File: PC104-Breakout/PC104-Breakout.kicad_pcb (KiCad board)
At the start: 4 copper layers, 175 x 100 mm, 21 parts, among them J1 Screw_Terminal_01x02, J2 Screw_Terminal_01x02, J3 Screw_Terminal_01x02, M1 MountingHole_Pad, M2 MountingHole_Pad, M3 MountingHole_Pad, M4 MountingHole_Pad, M5 MountingHole_Pad, M6 MountingHole_Pad, M7 MountingHole_Pad, M8 MountingHole_Pad

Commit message: Added silkscreen - created production files
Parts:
- added G***: LOGO, LOGO, B.Cu at (208.2, 95.7)
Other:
- board text added: "2024-05-20"
- board text added: "Rev 1"

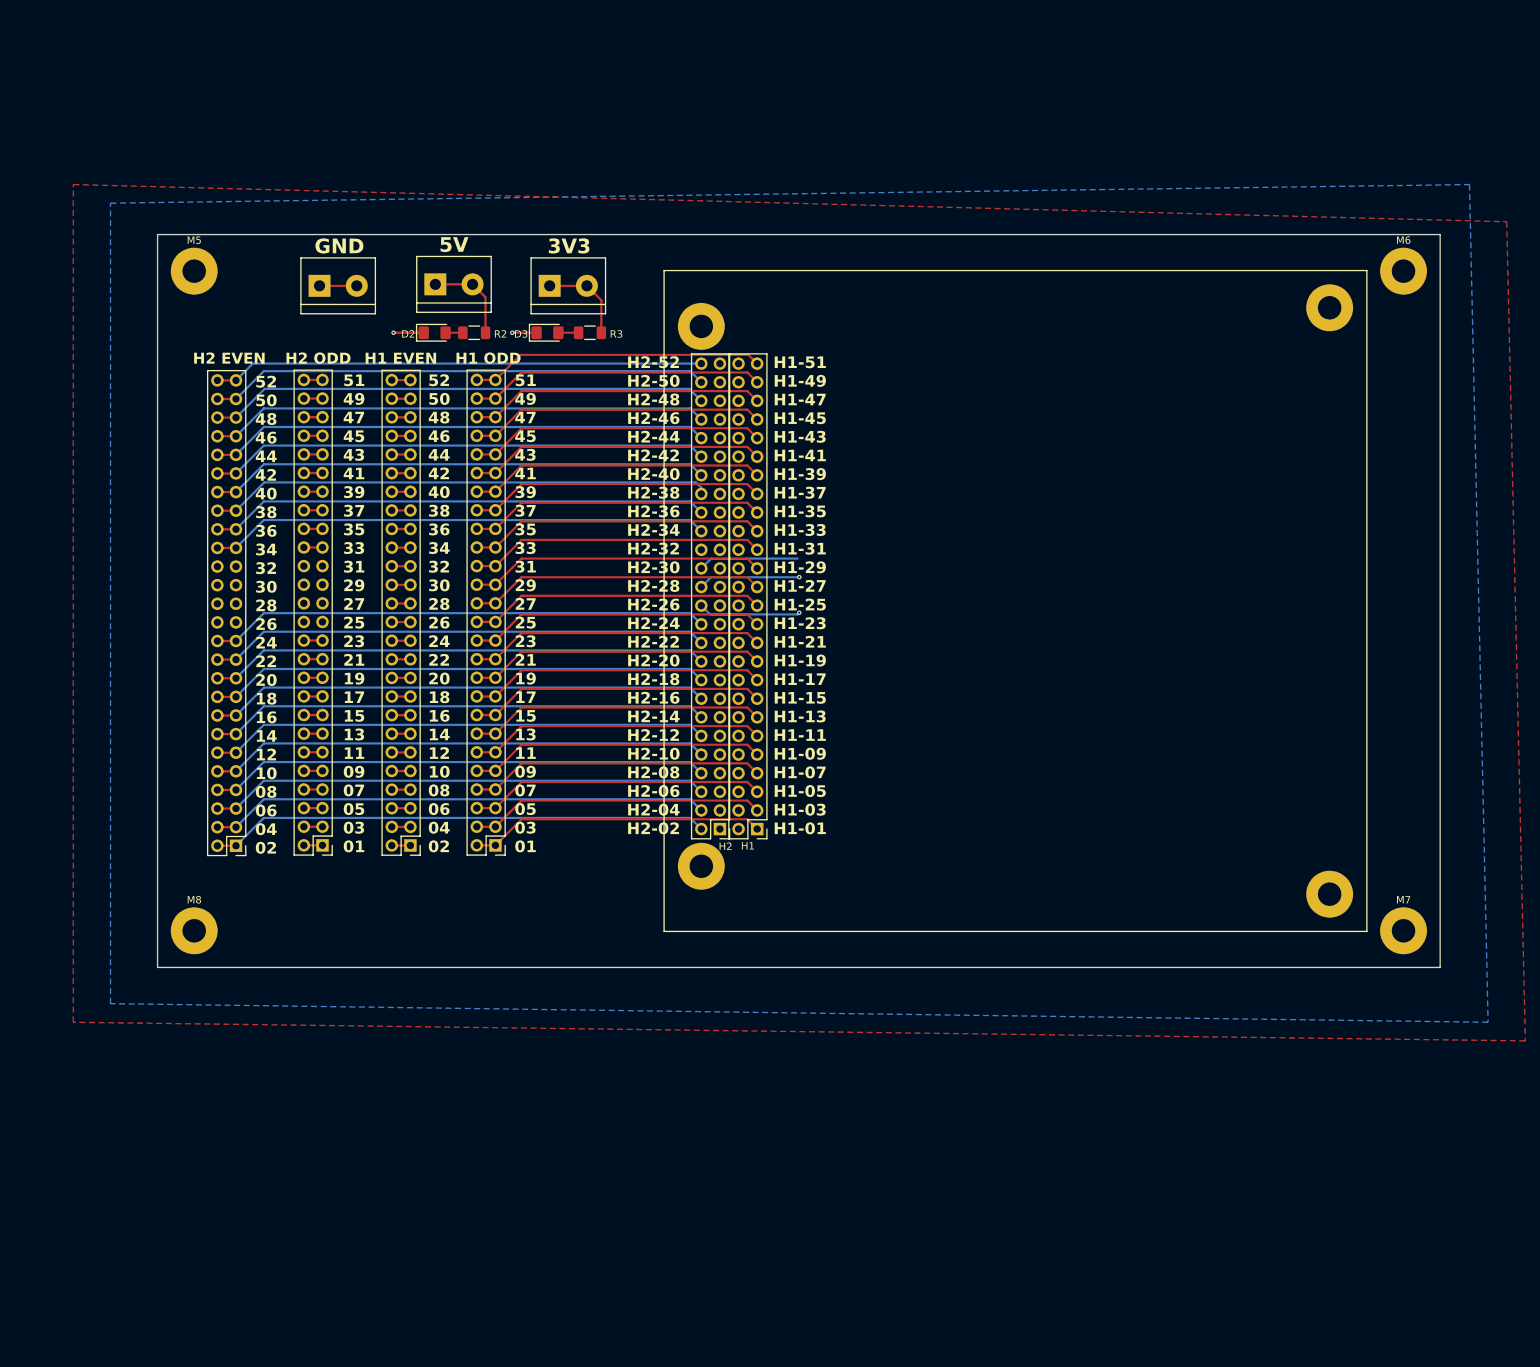
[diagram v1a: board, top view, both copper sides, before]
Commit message: Reorganized PCB layout
Modified layout files to change board from 4 layers to 2 in order to decrease production costs by $45. Shifted two stack headers to the right of the space allocated for the EPS and rerouted with 2 layers. Created polygons for GND and 3V3 nets.
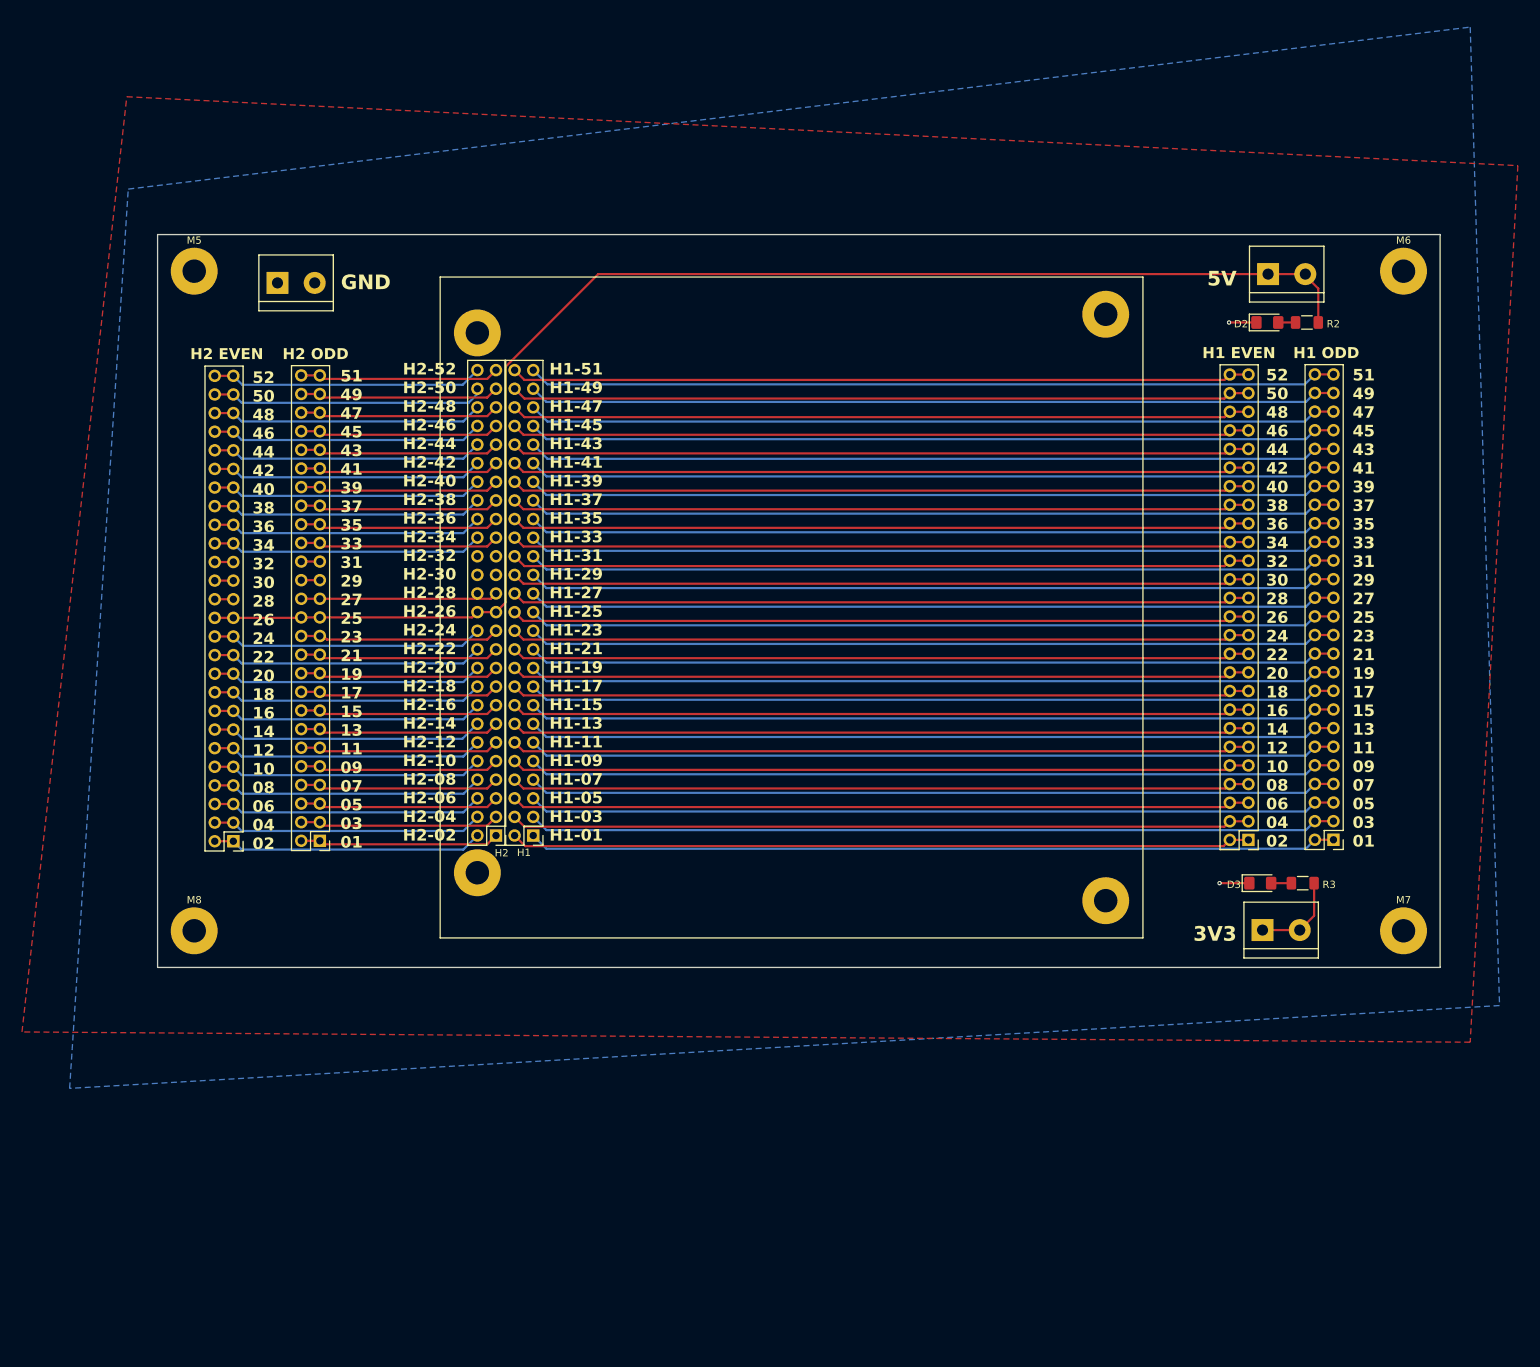
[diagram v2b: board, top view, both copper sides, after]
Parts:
- moved J3 131.1 mm to (225.8, 144.9)
- moved D3 122.9 mm to (225.4, 138.5)
- moved R3 122.9 mm to (231.2, 138.5)
- moved H1E1 114.3 mm to (223.8, 132.6)
- moved H1O1 114.3 mm to (235.4, 132.6)
- moved J2 113.6 mm to (226.5, 55.4)
- moved D2 113.6 mm to (226.4, 62.0)
- moved R2 113.6 mm to (231.8, 62.0)
- moved G*** 30.6 mm to (177.6, 96.6)
- moved H1 30.6 mm to (126.3, 132.0)
- moved H2 30.6 mm to (121.2, 132.0)
- moved M1 30.6 mm to (118.6, 63.4)
- moved M4 30.6 mm to (118.6, 137.1)
- moved M2 30.6 mm to (204.4, 60.9)
- moved M3 30.6 mm to (204.4, 140.9)
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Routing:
- net H2-25: track 26.4 -> 194.4 mm, vias 1 -> 0
- net H1-51: track 40.2 -> 110.6 mm
- net H1-43: track 40.3 -> 110.6 mm
- net H1-47: track 40.3 -> 110.6 mm
- net H1-07: track 40.3 -> 110.4 mm
- net H1-39: track 40.3 -> 110.4 mm
- net H1-49: track 40.3 -> 110.4 mm
- net H1-45: track 40.3 -> 110.4 mm
- net H1-37: track 40.3 -> 110.4 mm
- net H1-35: track 40.3 -> 110.4 mm
- net H1-33: track 40.3 -> 110.4 mm
- net H1-31: track 40.3 -> 110.4 mm
- net H1-29: track 40.3 -> 110.4 mm
- net H1-27: track 40.3 -> 110.4 mm
- net H1-25: track 40.3 -> 110.4 mm
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- added copper zone on F.Cu, net H2-27
- removed copper zone on F.Cu, net H2-25
- removed copper zone on In1.Cu, net H2-27
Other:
- copper layers 4 -> 2

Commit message: Completed layout, updated silkscreen and added aesthetic fixes
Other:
- board text added: "2024-05-21"
- board text added: "Rev 2"
- board text removed: "2024-05-20"
- board text removed: "Rev 1"
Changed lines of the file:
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@@
 		(layer "Edge.Cuts")
 	)
-	(gr_text "2024-05-20\n"
+	(gr_text "2024-05-21\n"
 		(at 189.645 116.485 0)
 		(layer "B.SilkS")
@@
 		)
 	)
-	(gr_text "Rev 1"
-		(at 181.245 109.685 0)
+	(gr_text "Rev 2"
+		(at 181.245 108.7 0)
 		(layer "B.SilkS")
 		(effects

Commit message: Created production files
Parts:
- removed the G*** at (177.6, 96.6)
- added G***: LOGO, PC104-Breakout-Lib:CTS-Logo-50x25, B.Cu at (175.9, 95.0)
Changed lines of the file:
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@@
 		)
 	)
-	(footprint "LOGO"
+	(footprint "PC104-Breakout-Lib:CTS-Logo-50x25"
 		(layer "B.Cu")
-		(at 177.614973 96.585639 180)
+		(at 175.9 95 180)
 		(property "Reference" "G***"
 			(at 0 0 180)
@@
 			)
 		)
-		(property "Footprint" ""
+		(property "Footprint" "PC104-Breakout-Lib:CTS-Logo-50x25"
 			(at 0 0 0)
 			(unlocked yes)
@@
 	)
 	(gr_text "Rev 2"
-		(at 181.245 108.7 0)
+		(at 181.245 108.4 0)
 		(layer "B.SilkS")
 		(effects
@@
 	)
 	(segment
-		(start 122.515 68.002943)
-		(end 135.117943 55.4)
-		(width 0.3)
+		(start 226.52 55.4)
+		(end 134.8 55.4)
+		(width 1)
 		(layer "F.Cu")
 		(net 56)
 	)
 	(segment
-		(start 231.6 55.6)
-		(end 233.37 57.37)
+		(start 122.515 68.002943)
+		(end 122.515 67.685)
 		(width 0.3)
 		(layer "F.Cu")
@@
 	)
 	(segment
-		(start 226.52 55.4)
+		(start 233.37 57.17)
 		(end 231.6 55.4)
 		(width 0.3)
@@
 	)
 	(segment
-		(start 135.117943 55.4)
-		(end 226.52 55.4)
-		(width 0.3)
+		(start 134.8 55.4)
+		(end 125.1 65.1)
+		(width 1)
 		(layer "F.Cu")
 		(net 56)
@@
 	)
 	(segment
-		(start 233.37 57.37)
-		(end 233.37 62)
+		(start 231.6 55.4)
+		(end 226.52 55.4)
+		(width 1)
+		(layer "F.Cu")
+		(net 56)
+	)
+	(segment
+		(start 122.515 67.685)
+		(end 125.1 65.1)
 		(width 0.3)
 		(layer "F.Cu")
@@
 	)
 	(segment
+		(start 233.37 62)
+		(end 233.37 57.17)
+		(width 0.3)
+		(layer "F.Cu")
+		(net 56)
+	)
+	(segment
 		(start 117.915 102.24)
 		(end 118.635 101.52)
@@
 	)
 	(segment
-		(start 230.27 62)
-		(end 227.9075 62)
+		(start 227.9075 62)
+		(end 230.27 62)
 		(width 0.3)
 		(layer "F.Cu")

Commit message: Update for Rev 3, do layout
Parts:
- removed G***: LOGO, PC104-Breakout-Lib:CTS-Logo-50x25
- removed the J1 at (91.4, 56.6)
- removed the J2 at (226.5, 55.4)
- removed the J3 at (225.8, 144.9)
- added D1: LED, LED_SMD:LED_0603_1608Metric_Pad1.05x0.95mm_HandSolder, F.Cu at (220.6, 64.0)
- added D4: LED, LED_SMD:LED_0603_1608Metric_Pad1.05x0.95mm_HandSolder, F.Cu at (220.6, 71.8)
- added D5: LED, LED_SMD:LED_0603_1608Metric_Pad1.05x0.95mm_HandSolder, F.Cu at (220.6, 74.4)
- added D6: LED, LED_SMD:LED_0603_1608Metric_Pad1.05x0.95mm_HandSolder, F.Cu at (220.6, 77.0)
- added J4: Screw_Terminal_01x02, TerminalBlock:TerminalBlock_bornier-2_P5.08mm, F.Cu at (246.0, 143.5)
- added J5: Screw_Terminal_01x02, TerminalBlock:TerminalBlock_bornier-2_P5.08mm, F.Cu at (246.0, 108.0)
- added J6: Screw_Terminal_01x02, TerminalBlock:TerminalBlock_bornier-2_P5.08mm, F.Cu at (246.0, 72.0)
- added J7: Conn_01x02, Connector_PinHeader_2.54mm:PinHeader_1x03_P2.54mm_Vertical, F.Cu at (238.0, 143.5)
- added J8: Conn_01x02, Connector_PinHeader_2.54mm:PinHeader_1x03_P2.54mm_Vertical, F.Cu at (238.0, 108.5)
- added J9: Conn_01x02, Connector_PinHeader_2.54mm:PinHeader_1x03_P2.54mm_Vertical, F.Cu at (238.0, 72.0)
- added LG1: MountingHole, PC104-Breakout-Lib:CTS-Logo-50x25, B.Cu at (173.0, 93.0)
- added LG2: MountingHole, PC104-Breakout-Lib:CTS-Logo-50x25, F.Cu at (170.9, 92.5)
- added M10: MountingHole_Pad, MountingHole:MountingHole_3.2mm_M3_Pad, F.Cu at (213.0, 140.0)
- added M11: MountingHole_Pad, MountingHole:MountingHole_3.2mm_M3_Pad, F.Cu at (213.0, 61.0)
- added M12: MountingHole_Pad, MountingHole:MountingHole_3.2mm_M3_Pad, F.Cu at (110.0, 63.0)
- added M9: MountingHole_Pad, MountingHole:MountingHole_3.2mm_M3_Pad, F.Cu at (110.0, 140.0)
- added R1: 10k, Resistor_SMD:R_0603_1608Metric_Pad0.98x0.95mm_HandSolder, F.Cu at (85.0, 53.0)
- added R10: 5k1, Resistor_SMD:R_0603_1608Metric_Pad0.98x0.95mm_HandSolder, F.Cu at (224.9, 66.5)
- added R11: 3k3, Resistor_SMD:R_0603_1608Metric_Pad0.98x0.95mm_HandSolder, F.Cu at (224.9, 69.0)
- added R12: 3k3, Resistor_SMD:R_0603_1608Metric_Pad0.98x0.95mm_HandSolder, F.Cu at (224.9, 71.5)
- added R13: 10k, Resistor_SMD:R_0603_1608Metric_Pad0.98x0.95mm_HandSolder, F.Cu at (224.9, 74.0)
- added R14: 10k, Resistor_SMD:R_0603_1608Metric_Pad0.98x0.95mm_HandSolder, F.Cu at (224.9, 76.5)
- added R4: 10k, Resistor_SMD:R_0603_1608Metric_Pad0.98x0.95mm_HandSolder, F.Cu at (80.0, 169.0)
- added R5: 10k, Resistor_SMD:R_0603_1608Metric_Pad0.98x0.95mm_HandSolder, F.Cu at (110.0, 145.0)
- added R6: 10k, Resistor_SMD:R_0603_1608Metric_Pad0.98x0.95mm_HandSolder, F.Cu at (213.0, 135.0)
- added R7: 10k, Resistor_SMD:R_0603_1608Metric_Pad0.98x0.95mm_HandSolder, F.Cu at (213.0, 56.0)
- added R8: 10k, Resistor_SMD:R_0603_1608Metric_Pad0.98x0.95mm_HandSolder, F.Cu at (110.0, 58.0)
- added R9: 5k1, Resistor_SMD:R_0603_1608Metric_Pad0.98x0.95mm_HandSolder, F.Cu at (224.9, 64.0)
- added TP1: TestPoint, PC104-Breakout-Lib:EdgeAlligatorConnector, F.Cu at (236.0, 163.0)
- added TP2: TestPoint, PC104-Breakout-Lib:EdgeAlligatorConnector, F.Cu at (235.5, 128.0)
- added TP3: TestPoint, PC104-Breakout-Lib:EdgeAlligatorConnector, F.Cu at (235.5, 92.0)
- added TP4: TestPoint, PC104-Breakout-Lib:EdgeAlligatorConnector, F.Cu at (236.0, 152.0)
- added TP5: TestPoint, PC104-Breakout-Lib:EdgeAlligatorConnector, F.Cu at (235.5, 117.0)
- added TP6: TestPoint, PC104-Breakout-Lib:EdgeAlligatorConnector, F.Cu at (235.5, 81.0)
- D2, D3: value D -> LED; footprint Diode_SMD:D_1206_3216Metric_Pad1.42x1.75mm_HandSolder -> LED_SMD:LED_0603_1608Metric_Pad1.05x0.95mm_HandSolder
- R2: value 3.3k -> 10k; footprint Resistor_SMD:R_1206_3216Metric_Pad1.30x1.75mm_HandSolder -> Resistor_SMD:R_0603_1608Metric_Pad0.98x0.95mm_HandSolder
- R3: value 2.2k -> 10k; footprint Resistor_SMD:R_1206_3216Metric_Pad1.30x1.75mm_HandSolder -> Resistor_SMD:R_0603_1608Metric_Pad0.98x0.95mm_HandSolder
- moved J3 79.6 mm to (155.5, 170.5), turned to -90 degrees
- moved D3 69.5 mm to (220.6, 69.2)
- moved H3 63.0 mm to (155.5, 156.5), turned to -90 degrees
- moved J1 38.6 mm to (231.5, 170.5), turned to -90 degrees
- moved R3 36.6 mm to (240.0, 174.0), turned to 90 degrees
- moved M7 29.0 mm to (245.0, 174.0)
- moved M8 29.0 mm to (80.0, 174.0)
- moved J2 24.2 mm to (231.5, 156.5), turned to -90 degrees
- moved R2 12.2 mm to (240.0, 53.0), turned to 90 degrees
- moved D2 7.45 mm to (220.6, 66.6)
- moved M5 2.00 mm to (80.0, 53.0)
- moved M6 2.00 mm to (245.0, 53.0)
- renumbered H2 to H1, H1 to H2, H2O1 to H3, H1E1 to J1, H1O1 to J2, H2E1 to J3, M4 to M3, M3 to M4
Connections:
- H1 pad 26: H2-25 -> H2-26
- H1 pad 28: H2-27 -> H2-28
- H1 pad 30: H2-29 -> H2-30
- H1 pad 31: H2-29 -> H2-31
- H1 pad 32: H2-29 -> H2-32
- H3 pad 31: H2-29 -> H2-31
- H3 pad 32: H2-29 -> H2-31
- J3 pad 25: H2-25 -> H2-26
- J3 pad 26: H2-25 -> H2-26
- J3 pad 27: H2-27 -> H2-28
- J3 pad 28: H2-27 -> H2-28
- J3 pad 29: H2-29 -> H2-30
- J3 pad 30: H2-29 -> H2-30
- J3 pad 31: H2-29 -> H2-32
- J3 pad 32: H2-29 -> H2-32
- M5 pad 1: unconnected-(M5-Pad1) -> Net-(M5-Pad1)
- M6 pad 1: unconnected-(M6-Pad1) -> Net-(M6-Pad1)
- M7 pad 1: unconnected-(M7-Pad1) -> Net-(M7-Pad1)
- M8 pad 1: unconnected-(M8-Pad1) -> Net-(M8-Pad1)
- R2 pad 1: H2-25 -> Net-(M6-Pad1)
- R2 pad 2: Net-(D2-A) -> H2-29
- R3 pad 1: H2-27 -> Net-(M7-Pad1)
- R3 pad 2: Net-(D3-A) -> H2-29
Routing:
- net H2-25: track 194.8 -> 0.00 mm
- net H1-51: track 110.6 -> 0.00 mm
- net H1-43: track 110.6 -> 0.00 mm
- net H1-47: track 110.6 -> 0.00 mm
- net H1-07: track 110.4 -> 0.00 mm
- net H1-39: track 110.4 -> 0.00 mm
- net H1-49: track 110.4 -> 0.00 mm
- net H1-45: track 110.4 -> 0.00 mm
- net H1-41: track 110.4 -> 0.00 mm
- net H1-37: track 110.4 -> 0.00 mm
- net H1-35: track 110.4 -> 0.00 mm
- net H1-33: track 110.4 -> 0.00 mm
- net H1-31: track 110.4 -> 0.00 mm
- net H1-29: track 110.4 -> 0.00 mm
- net H1-27: track 110.4 -> 0.00 mm
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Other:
- board size 175 x 100 mm -> 175 x 131 mm
- board text added: "PC104 Breakout Rev 3 2025-02-02"
- board text removed: "2024-05-21"
- board text removed: "3V3"
- board text removed: "5V"
- board text removed: "GND"
- board text removed: "Rev 2"

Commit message: Polish 3d models, silkscreen
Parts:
- added D7: LED, LED_SMD:LED_0603_1608Metric_Pad1.05x0.95mm_HandSolder, F.Cu at (225.6, 86.5)
- added D8: LED, LED_SMD:LED_0603_1608Metric_Pad1.05x0.95mm_HandSolder, F.Cu at (225.6, 50.5)
- added J11: Conn_01x03_Socket, Connector_PinSocket_2.54mm:PinSocket_1x03_P2.54mm_Vertical, F.Cu at (234.0, 119.5)
- added J12: Conn_01x03_Socket, Connector_PinSocket_2.54mm:PinSocket_1x03_P2.54mm_Vertical, F.Cu at (234.0, 83.5)
- added J13: Conn_01x03_Socket, Connector_PinSocket_2.54mm:PinSocket_1x03_P2.54mm_Vertical, F.Cu at (234.0, 47.0)
- added R15: 5k1, Resistor_SMD:R_0603_1608Metric_Pad0.98x0.95mm_HandSolder, B.Cu at (225.6, 84.5)
- added R16: 3k3, Resistor_SMD:R_0603_1608Metric_Pad0.98x0.95mm_HandSolder, B.Cu at (225.8, 48.5)
- H1: renamed from H2; footprint Connector_PinHeader_2.54mm:PinHeader_2x26_P2.54mm_Vertical -> PC104-Breakout-Lib:PinSocket_2x26_P2.54mm_Vertical_TightPlacement
- H2: renamed from H1; footprint Connector_PinHeader_2.54mm:PinHeader_2x26_P2.54mm_Vertical -> PC104-Breakout-Lib:PinSocket_2x26_P2.54mm_Vertical_TightPlacement
- J1, J2, J3: footprint Connector_PinHeader_2.54mm:PinHeader_2x26_P2.54mm_Vertical -> PC104-Breakout-Lib:PinHeader_2x26_P2.54mm_Vertical_HeaderAndSocket
- J4: renamed from H3; footprint Connector_PinHeader_2.54mm:PinHeader_2x26_P2.54mm_Vertical -> PC104-Breakout-Lib:PinHeader_2x26_P2.54mm_Vertical_HeaderAndSocket
- R1, R14, R2, R3, R4, R5, R6, R7, R8, R9: moved to B.Cu
- R10: renamed from R11; moved to B.Cu
- R11: renamed from R13; moved to B.Cu
- R12: renamed from R10; moved to B.Cu
- R13: renamed from R12; moved to B.Cu
- moved R14 142.0 mm to (85.0, 52.0)
- moved R13 140.4 mm to (85.0, 60.0)
- moved R12 139.9 mm to (85.0, 67.5)
- moved D-H2-46 138.2 mm to (85.0, 50.0)
- moved D-H2-28 136.3 mm to (85.0, 58.0)
- moved D-H2-26 135.6 mm to (85.0, 65.5)
- moved R11 131.8 mm to (95.0, 52.0)
- moved R10 130.2 mm to (95.0, 60.0)
- moved R9 130.0 mm to (95.0, 67.5)
- moved D-H2-45 127.9 mm to (95.0, 50.0)
- moved D-H2-27 126.1 mm to (95.0, 58.0)
- moved D-H2-25 125.6 mm to (95.0, 65.5)
- moved TP2 25.0 mm to (236.0, 103.0)
- moved TP3 25.0 mm to (236.0, 67.0)
- moved TP5 25.0 mm to (236.0, 92.0)
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- renumbered D1 to D-H2-25, D2 to D-H2-26, D3 to D-H2-27, D4 to D-H2-28, D5 to D-H2-45, D6 to D-H2-46, J9 to J10, J4 to J5, J5 to J6, J6 to J7, J7 to J8, J8 to J9
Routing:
- added copper zone on F.Cu, net H2-29
- removed copper zone on F.Cu, net H2-27
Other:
- board text added: "(H2-25)"
- board text added: "(H2-27)"
- board text added: "(H2-29)"
- board text added: "+3V3"
- board text added: "+5V"
- board text added: "3V3"
- board text added: "5V"
- board text added: "GND"
- board text added: "Pin Check LEDs"
- board text added: "Vbatt"
